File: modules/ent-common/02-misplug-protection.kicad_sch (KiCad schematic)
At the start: 6 parts

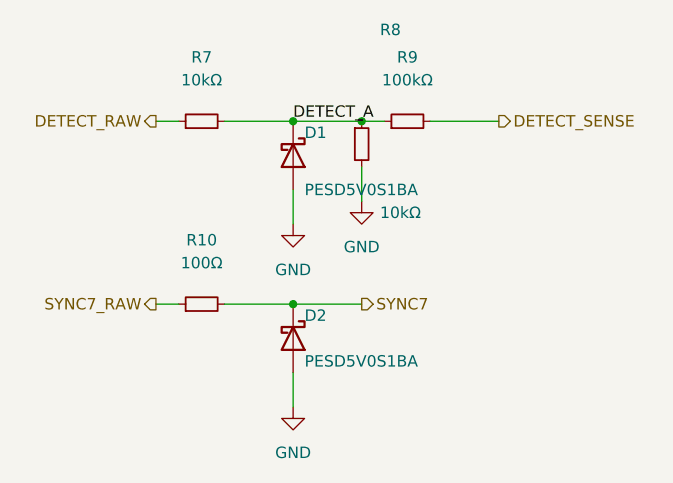
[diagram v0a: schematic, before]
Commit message: WIP snapshot: composition-standard agent in flight (durability)
Standard doc + layout/compose edits + ent-common regen in progress; hub
regen not yet run. NOTE for landing review: lib/cec-ent-power.kicad_sym
is modified — outside the declared scope fence; inspect the diff at
verification before accepting.

Co-Authored-By: Claude Fable 5 <noreply@anthropic.com>
Claude-Session: https://claude.ai/code/session_011q5bmwF5BFtSf8Ft5vT1DZ
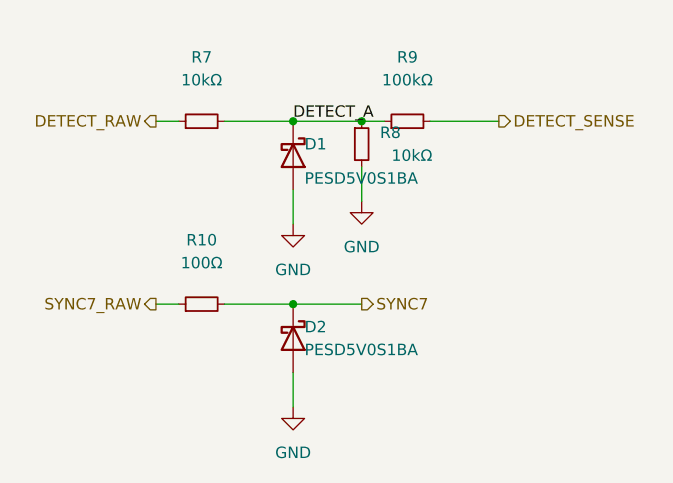
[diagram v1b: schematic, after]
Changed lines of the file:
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@@
 		(dnp no)
 		(fields_autoplaced yes)
-		(property "Reference" "D1" (at 139.7 88.9 90) (effects (font (size 1.27 1.27)) (justify left)))
-		(property "Value" "PESD5V0S1BA" (at 139.7 95.25 90) (effects (font (size 1.27 1.27)) (justify left)))
+		(property "Reference" "D1" (at 139.7 90.17 90) (effects (font (size 1.27 1.27)) (justify left)))
+		(property "Value" "PESD5V0S1BA" (at 139.7 93.98 90) (effects (font (size 1.27 1.27)) (justify left)))
 		(property "Footprint" "cec-Diode_SMD:D_SOD-323" (at 138.43 91.44 0) (effects (font (size 1.27 1.27)) (hide yes)))
 		(property "Datasheet" "" (at 138.43 91.44 0) (effects (font (size 1.27 1.27)) (hide yes)))
@@
 		(dnp no)
 		(fields_autoplaced yes)
-		(property "Reference" "R8" (at 148.082 77.47 0) (effects (font (size 1.27 1.27)) (justify left)))
-		(property "Value" "10kΩ" (at 148.082 97.79 0) (effects (font (size 1.27 1.27)) (justify left)))
+		(property "Reference" "R8" (at 148.082 88.9 0) (effects (font (size 1.27 1.27)) (justify left)))
+		(property "Value" "10kΩ" (at 149.352 91.44 0) (effects (font (size 1.27 1.27)) (justify left)))
 		(property "Footprint" "cec-Resistor_SMD:R_0402_1005Metric" (at 146.05 90.17 0) (effects (font (size 1.27 1.27)) (hide yes)))
 		(property "Datasheet" "" (at 146.05 90.17 0) (effects (font (size 1.27 1.27)) (hide yes)))
@@
 		(dnp no)
 		(fields_autoplaced yes)
-		(property "Reference" "D2" (at 139.7 109.22 90) (effects (font (size 1.27 1.27)) (justify left)))
-		(property "Value" "PESD5V0S1BA" (at 139.7 114.3 90) (effects (font (size 1.27 1.27)) (justify left)))
+		(property "Reference" "D2" (at 139.7 110.49 90) (effects (font (size 1.27 1.27)) (justify left)))
+		(property "Value" "PESD5V0S1BA" (at 139.7 113.03 90) (effects (font (size 1.27 1.27)) (justify left)))
 		(property "Footprint" "cec-Diode_SMD:D_SOD-323" (at 138.43 111.76 0) (effects (font (size 1.27 1.27)) (hide yes)))
 		(property "Datasheet" "" (at 138.43 111.76 0) (effects (font (size 1.27 1.27)) (hide yes)))

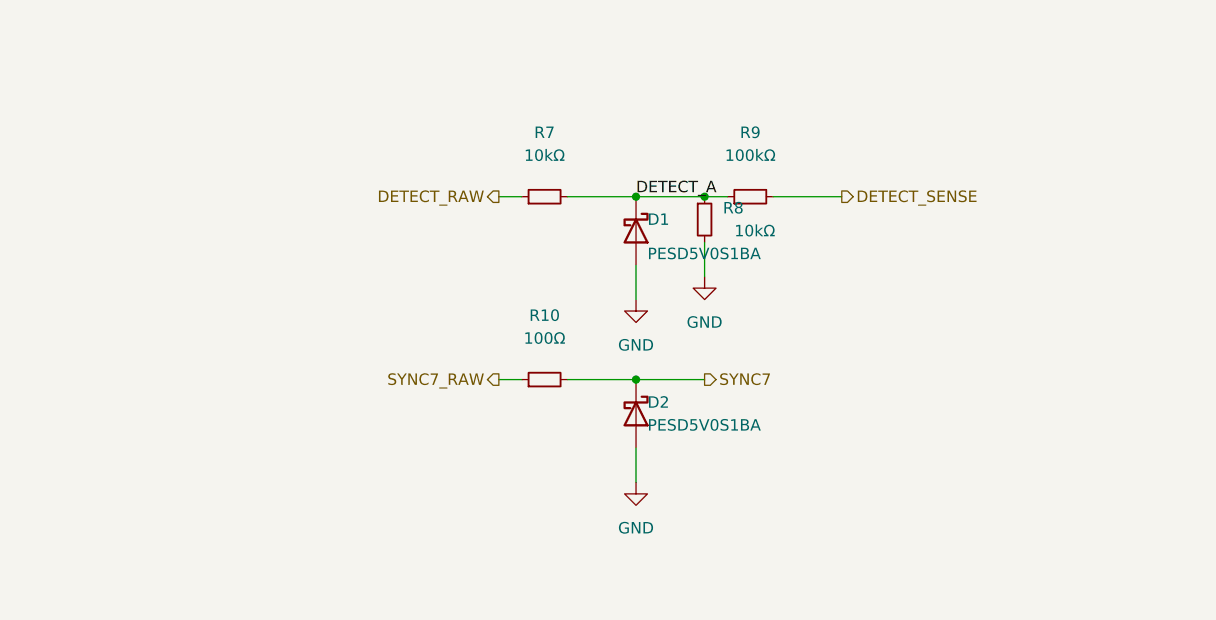
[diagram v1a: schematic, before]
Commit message: WIP snapshot: hygiene wave (consumer BOM/schematic props) + composition agent, both in flight (durability)
Co-Authored-By: Claude Fable 5 <noreply@anthropic.com>
Claude-Session: https://claude.ai/code/session_011q5bmwF5BFtSf8Ft5vT1DZ
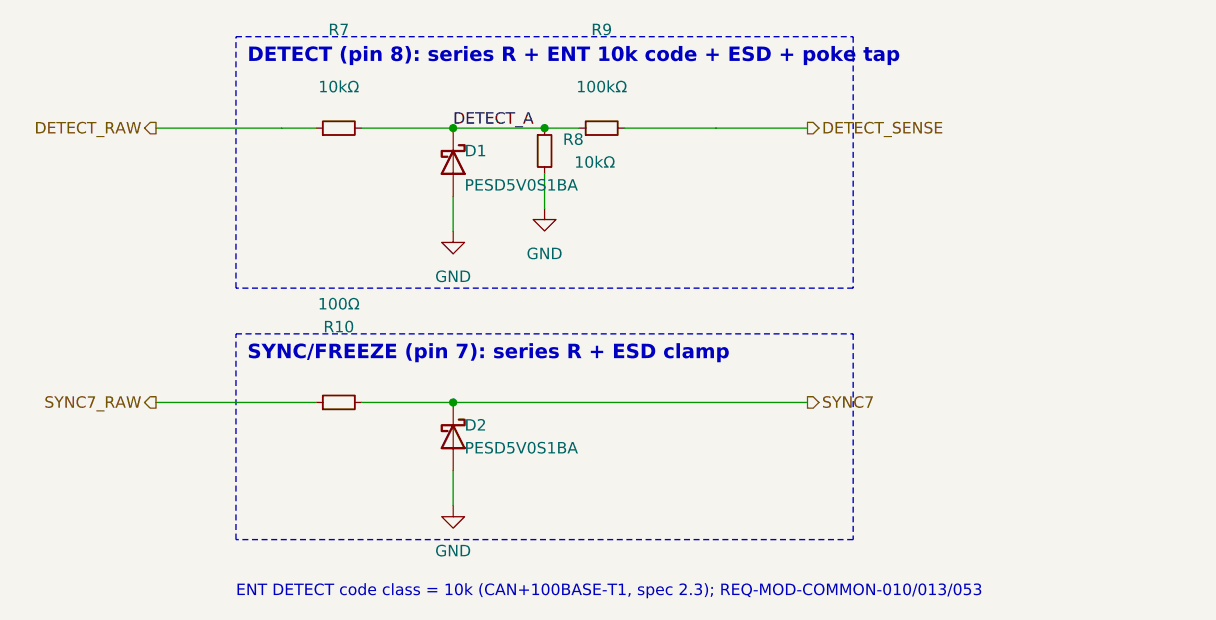
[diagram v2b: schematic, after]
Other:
- note added: "DETECT (pin 8): series R + ENT 10k code + ESD + poke tap"
- note added: "ENT DETECT code class = 10k (CAN+100BASE-T1, spec 2.3); REQ-MOD-COMMON-010/013/053"
- note added: "SYNC/FREEZE (pin 7): series R + ESD clamp"
- title: CEC ENT module common block: 02-misplug-protection -> SYNC/FREEZE (pin 7): series R + ESD clamp

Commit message: WIP snapshot: hygiene wave (rev3 manifest, EPS README) + composition agent, in flight (durability)
Co-Authored-By: Claude Fable 5 <noreply@anthropic.com>
Claude-Session: https://claude.ai/code/session_011q5bmwF5BFtSf8Ft5vT1DZ
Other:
- title: SYNC/FREEZE (pin 7): series R + ESD clamp -> CEC ENT module common block: 02-misplug-protection
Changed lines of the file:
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@@
 	(paper "A4")
 	(title_block
-		(title "SYNC/FREEZE (pin 7): series R + ESD clamp")
+		(title "CEC ENT module common block: 02-misplug-protection")
 		(date "2026-07-02")
 		(rev "DRAFT")
